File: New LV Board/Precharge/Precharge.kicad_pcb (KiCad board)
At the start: 2 copper layers, 83.2 x 41.2 mm, 33 parts, among them J1 Screw_Terminal_01x02, J2 Screw_Terminal_01x02, K1 G3VM-61G2, Q1 BSS214NW, Q2 MPSA42, Q4 IRLML5203, U1 LM2904, U3 NE555P, U4 LR8N3-G

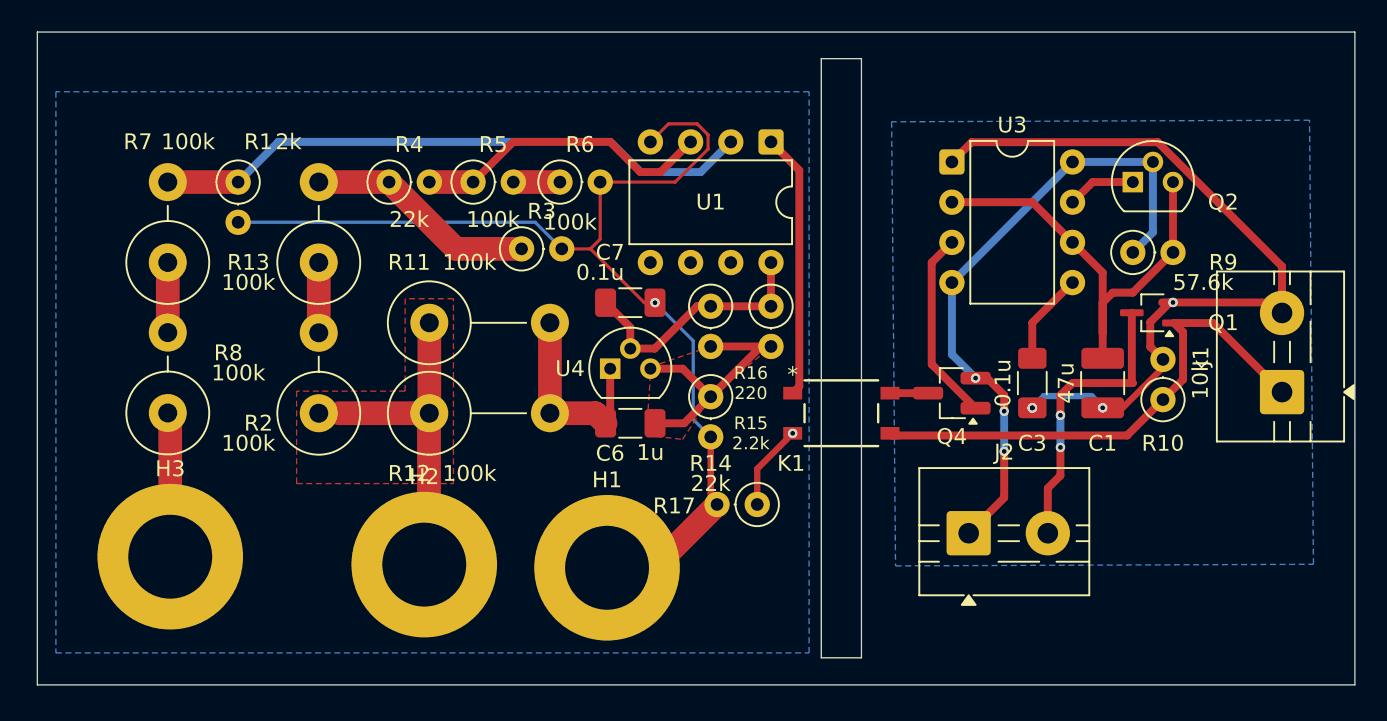
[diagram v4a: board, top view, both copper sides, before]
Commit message: minor changes for jlc
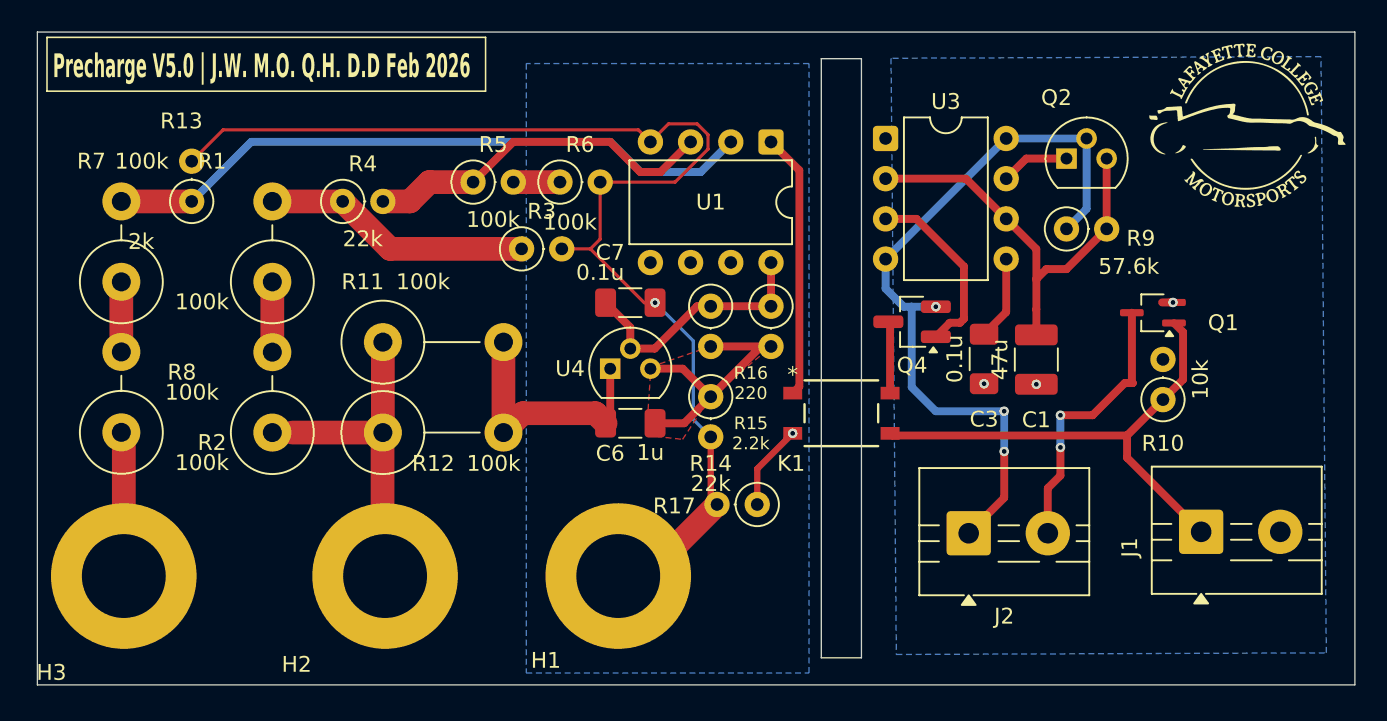
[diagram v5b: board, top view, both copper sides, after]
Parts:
- moved J1 10.2 mm to (94.5, 46.2), turned to 0 degrees
- moved Q4 5.16 mm to (76.2, 33.0)
- moved C1 4.45 mm to (84.1, 35.3)
- moved Q2 4.45 mm to (86.0, 22.6)
- moved R9 4.45 mm to (86.0, 27.1)
- moved U3 4.45 mm to (74.5, 21.4)
- moved C3 3.41 mm to (80.8, 35.3)
- moved H3 3.18 mm to (26.4, 49.0)
- moved R13 3.18 mm to (30.7, 25.4), turned to 90 degrees
- moved R8 3.18 mm to (26.3, 39.9)
- moved R7 3.18 mm to (26.3, 30.4)
- moved R12 3.18 mm to (42.8, 40.0)
- moved R2 3.18 mm to (35.8, 40.0)
- moved R4 3.18 mm to (40.2, 25.4)
- moved R1 3.18 mm to (35.8, 30.4)
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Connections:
- J1 pad GLV-: (no net) -> GLV-
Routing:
- net GLV-: track 50.6 -> 1.88 mm, vias 4 -> 3
- net HVPACK-: track 68.9 -> 77.9 mm
- net TSMS+: track 40.7 -> 47.8 mm
- net Net-(U4-IN): track 13.4 -> 16.9 mm
- net Net-(U1A--): track 38.2 -> 41.6 mm
- net Net-(U1A-+): track 19.1 -> 22.6 mm
- net Net-(R1-Pad2): track 14.6 -> 17.0 mm
- net Net-(Q4-D): track 2.41 -> 4.55 mm
- net Net-(Q2-C): track 28.9 -> 27.0 mm
- net AIR1-: track 18.4 -> 17.7 mm
- net Done: track 32.5 -> 31.9 mm
- net Net-(U3-CV): track 5.84 -> 5.33 mm
- removed copper zone on F.Cu, net HVPACK+
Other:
- board text added: "Precharge V5.0 | J.W. M.O. Q.H. D.D Feb 2026"
- board text removed: "${REFERENCE}"

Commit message: Fixed precharge circuit
problems with previous design (all my fault):

1 - capacitor for the linear voltage regulator was connected between Vin and Adj, should be between Vin and ground

2 - TS+ was being multiplied by 0.9 instead of HVPACK+

3 - no resistor on the discharge pin of the 555 timer

4 - 220 ohm resistor on linear voltage regulator would have made it output like 100V no bueno

5 - if im not mistaken pin 2 and 6 of the 555 weren't connected???

6 - some silkscreen stuff was ugly i guess so i fixed that
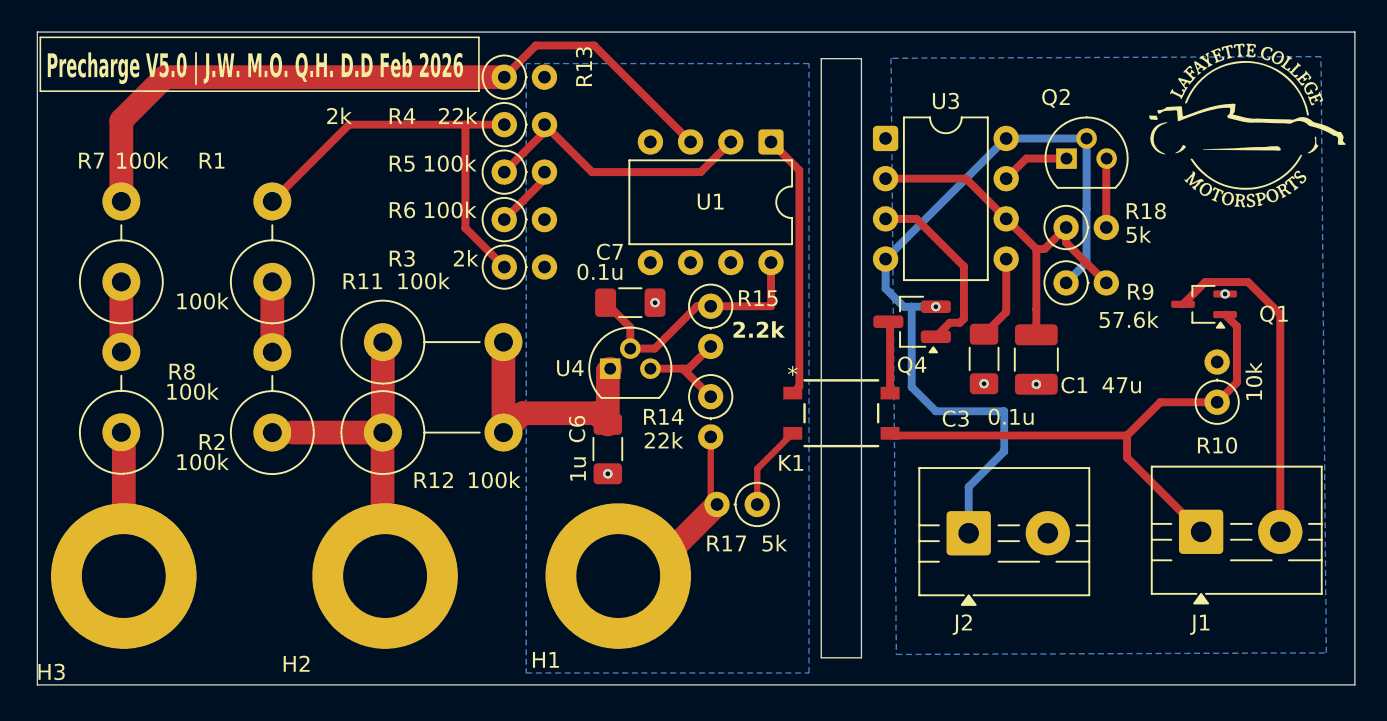
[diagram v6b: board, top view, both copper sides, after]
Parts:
- removed R16: 220, Resistor_THT:R_Axial_DIN0207_L6.3mm_D2.5mm_P2.54mm_Vertical
- added R18: 5k, Resistor_THT:R_Axial_DIN0207_L6.3mm_D2.5mm_P2.54mm_Vertical, F.Cu at (86.0, 27.0)
- U1: value LM2904 -> LM2903
- moved R13 21.3 mm to (50.5, 17.5), turned to 0 degrees
- moved R4 11.3 mm to (50.5, 20.5)
- moved R6 4.24 mm to (50.5, 26.5)
- moved R15 3.81 mm to (63.5, 32.0)
- moved R10 3.43 mm to (95.5, 38.0)
- moved R9 3.41 mm to (86.0, 30.5)
- moved Q1 3.27 mm to (94.7, 31.9)
- moved C6 2.16 mm to (57.0, 41.0), turned to -90 degrees
- moved R5 2.07 mm to (50.5, 23.5)
- moved R3 1.58 mm to (50.5, 29.5)
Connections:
- C1 pad 1: Net-(Q2-C) -> Net-(U3-THR)
- C6 pad 2: Net-(U4-ADJ) -> HVPACK-
- J2 pad 2: AIR1- -> GLV-
- R13 pad 1: Net-(U1A--) -> Net-(U1A-+)
- R4 pad 2: Net-(U1A-+) -> Net-(U1A--)
- R5 pad 1: Net-(U1A-+) -> Net-(U1A--)
- R7 pad 2: Net-(U1A--) -> Net-(U1A-+)
- R9 pad 2: Net-(Q2-C) -> Net-(U3-THR)
- U3 pad 2: Net-(Q2-C) -> Net-(U3-THR)
- U3 pad 6: Net-(Q2-C) -> Net-(U3-THR)
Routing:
- net HVPACK-: track 77.9 -> 13.0 mm, vias 1 -> 2
- net Net-(U1A--): track 41.6 -> 17.9 mm
- net Net-(U3-THR): track 0.00 -> 23.8 mm
- net Net-(U1A-+): track 22.6 -> 45.6 mm
- net Net-(Q2-C): track 27.0 -> 4.37 mm
- net Net-(U4-ADJ): track 17.7 -> 6.90 mm
- net Net-(R1-Pad2): track 17.0 -> 26.7 mm
- net Done: track 31.9 -> 36.0 mm
- net AIR1-: track 17.7 -> 21.3 mm, vias 2 -> 0
- net TSMS+: track 47.8 -> 51.2 mm, vias 3 -> 1
- net GLV-: track 1.88 -> 0.43 mm
- net Net-(R5-Pad2): track 2.95 -> 4.05 mm
- net Net-(U4-IN): track 16.9 -> 17.5 mm
- net Net-(K1-Pad2): vias 1 -> 0
- removed copper zone on F.Cu, net Net-(U4-ADJ)
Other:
- board text added: "*"

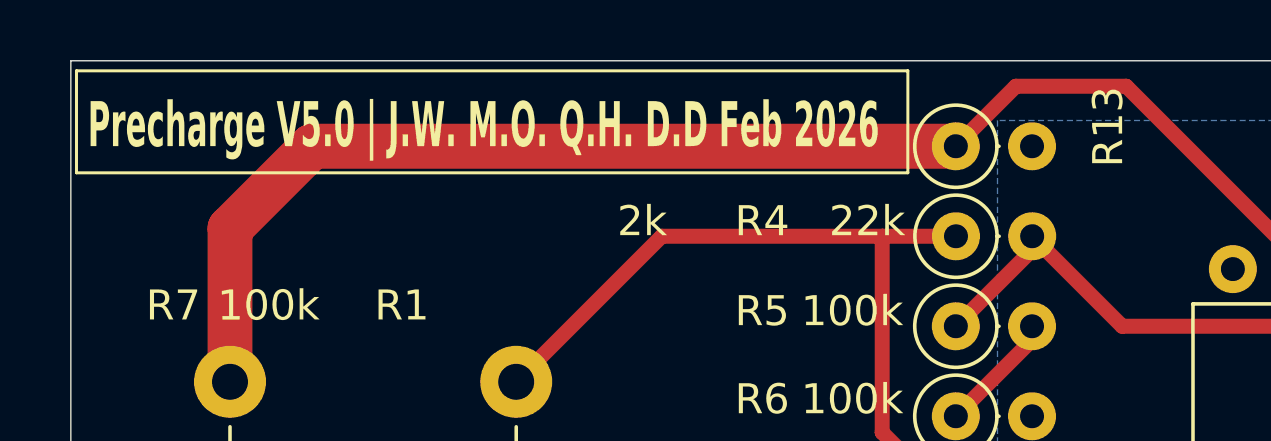
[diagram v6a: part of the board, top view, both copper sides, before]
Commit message: AMS & IMD fixing some connections
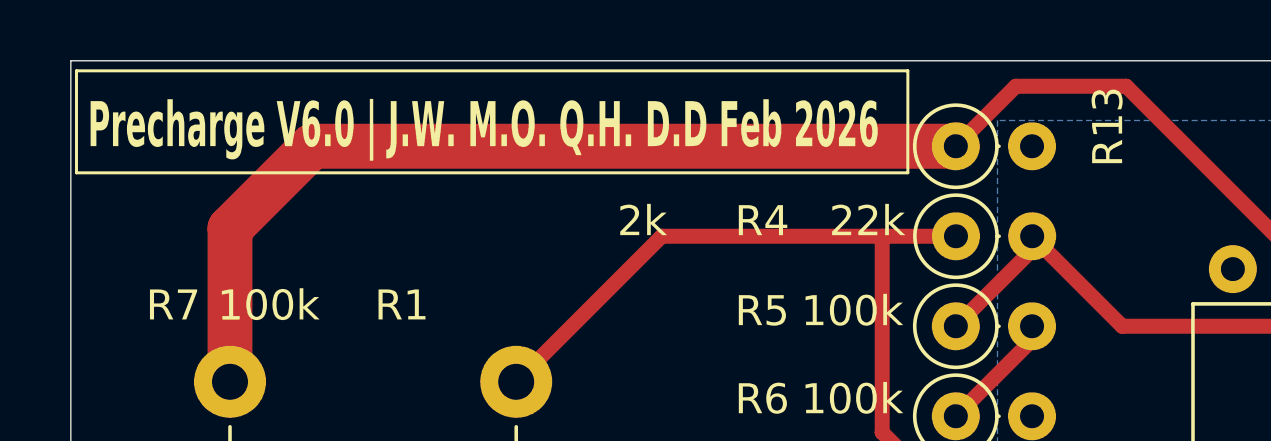
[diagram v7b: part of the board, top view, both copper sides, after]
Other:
- board text added: "Precharge V6.0 | J.W. M.O. Q.H. D.D Feb 2026"
- board text removed: "Precharge V5.0 | J.W. M.O. Q.H. D.D Feb 2026"
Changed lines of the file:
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@@
 		(layer "Edge.Cuts")
 	)
-	(gr_text "Precharge V5.0 | J.W. M.O. Q.H. D.D Feb 2026"
+	(gr_text "Precharge V6.0 | J.W. M.O. Q.H. D.D Feb 2026"
 		(at 21.519319 17.678899 0)
 		(layer "F.SilkS")

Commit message: merge
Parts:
- Q2: value MPSA42 -> SS8550; footprint Package_TO_SOT_THT:TO-92 -> Package_TO_SOT_THT:TO-92_Inline
- moved Q2 2.53 mm to (88.5, 22.5), turned to 180 degrees
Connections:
- R18 pad 2: Net-(Q2-C) -> Net-(Q2-E)
- U3 pad 7: Net-(Q2-E) -> Net-(Q2-C)
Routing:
- net TSMS+: track 51.2 -> 52.7 mm
- net Net-(Q2-E): track 4.34 -> 5.37 mm
